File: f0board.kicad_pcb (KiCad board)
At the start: 2 copper layers, 31 x 18.3 mm, 26 parts, among them P1 CONN_12, P2 CONN_12, SW1 SW_PUSH, U1 STM32F303CCT6, U2 MCP1700, U3 MAX3051, X1 XTAL-SMD-4-PADS

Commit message: Add dimensioning.
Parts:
- moved CONN2 20.4 mm to (84.8, 87.4)
- moved U3 8.27 mm to (95.2, 82.5)
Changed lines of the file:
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@@
     (links 90)
     (no_connects 90)
-    (area 0 0 0 0)
+    (area 84.988999 57.2262 139.960595 96.841001)
     (thickness 1.6)
-    (drawings 4)
+    (drawings 6)
     (tracks 0)
     (zones 0)
@@
   )
   (module _connectors:_Molex-PicoBlade-SMD-4 (layer F.Cu)
-    (at 86.868 67.056 270)
+    (at 84.836 87.376 270)
     (fp_text reference CONN2 (at 0 -0.8 270) (layer F.SilkS)
       (effects (font (size 0.5 0.5) (thickness 0.125)))
@@
   )
   (module _std:_SOT23-8 (layer F.Cu)
-    (at 94.6785 74.295)
+    (at 95.25 82.55)
     (fp_text reference U3 (at 0.9 -1.8) (layer F.SilkS)
       (effects (font (size 0.5 0.5) (thickness 0.125)))
@@
       (net 5 "Net-(C9-Pad1)"))
   )
+  (dimension 30.988 (width 0.3) (layer Cmts.User)
+    (gr_text "30.988 mm" (at 116.84 55.038) (layer Cmts.User)
+      (effects (font (size 1.5 1.5) (thickness 0.3)))
+    )
+    (feature1 (pts (xy 132.334 59.436) (xy 132.334 53.688)))
+    (feature2 (pts (xy 101.346 59.436) (xy 101.346 53.688)))
+    (crossbar (pts (xy 101.346 56.388) (xy 132.334 56.388)))
+    (arrow1a (pts (xy 132.334 56.388) (xy 131.207496 56.974421)))
+    (arrow1b (pts (xy 132.334 56.388) (xy 131.207496 55.801579)))
+    (arrow2a (pts (xy 101.346 56.388) (xy 102.472504 56.974421)))
+    (arrow2b (pts (xy 101.346 56.388) (xy 102.472504 55.801579)))
+  )
+  (dimension 18.288 (width 0.3) (layer Cmts.User)
+    (gr_text "18.288 mm" (at 97.202 68.58 90) (layer Cmts.User)
+      (effects (font (size 1.5 1.5) (thickness 0.3)))
+    )
+    (feature1 (pts (xy 101.346 59.436) (xy 95.852 59.436)))
+    (feature2 (pts (xy 101.346 77.724) (xy 95.852 77.724)))
+    (crossbar (pts (xy 98.552 77.724) (xy 98.552 59.436)))
+    (arrow1a (pts (xy 98.552 59.436) (xy 99.138421 60.562504)))
+    (arrow1b (pts (xy 98.552 59.436) (xy 97.965579 60.562504)))
+    (arrow2a (pts (xy 98.552 77.724) (xy 99.138421 76.597496)))
+    (arrow2b (pts (xy 98.552 77.724) (xy 97.965579 76.597496)))
+  )
   (gr_line (start 101.346 77.724) (end 101.346 59.436) (angle 90) (layer Edge.Cuts) (width 0.1))

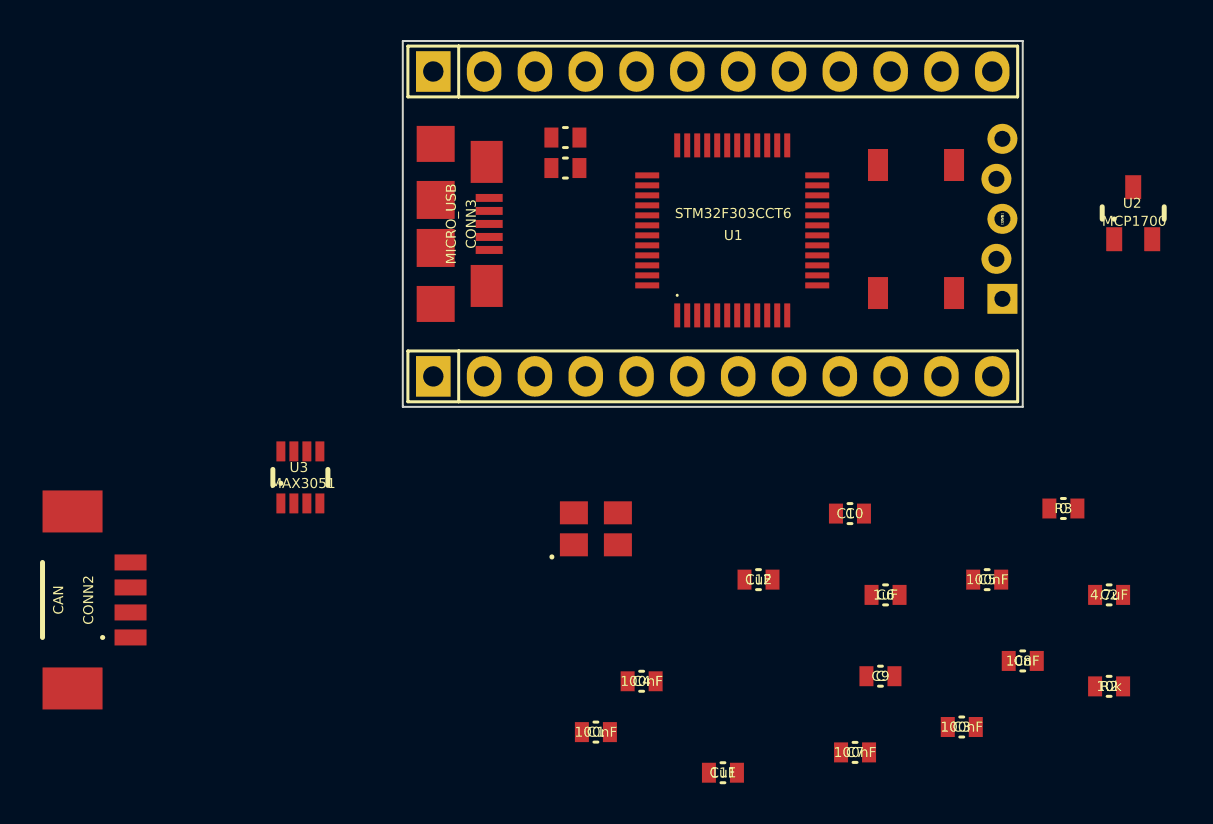
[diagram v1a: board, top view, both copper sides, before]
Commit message: placing/routing, change pinorder, add diode.
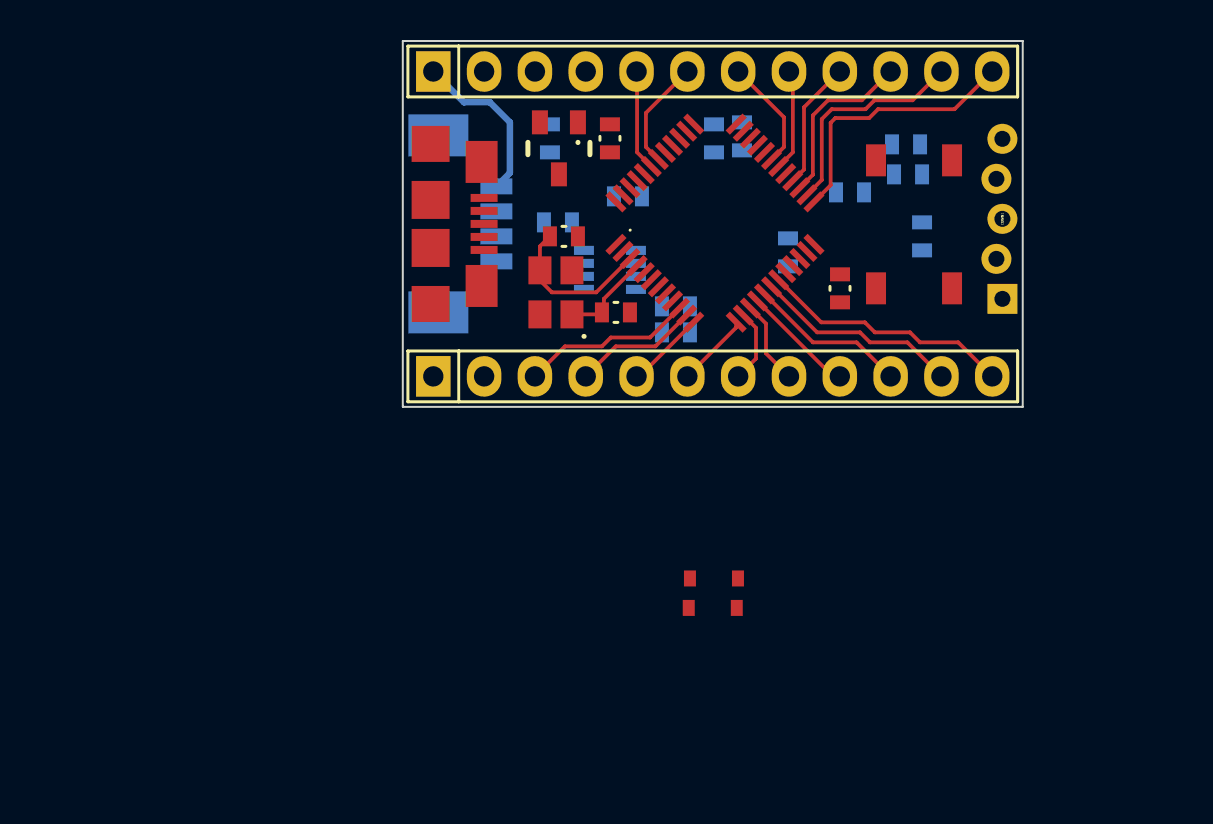
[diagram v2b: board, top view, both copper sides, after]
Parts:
- added D2: BAT60JFILM, _std:_SOD-323, F.Cu at (116.9, 86.3)
- added D3: BAT60JFILM, _std:_SOD-323, F.Cu at (116.8, 87.8)
- C1, C11, C2, C3, C4, C5, C6, C7, C8, CONN2, R1, R2, R3, U3: moved to B.Cu
- moved C1 33.2 mm to (126.5, 64.6)
- moved C11 32.9 mm to (108.7, 64.3), turned to 270 degrees
- moved C3 31.9 mm to (116.9, 64.3), turned to 270 degrees
- moved C7 30.0 mm to (112.6, 67.2)
- moved C2 29.4 mm to (118.3, 64.2), turned to 270 degrees
- moved R3 29.0 mm to (109.1, 68.5), turned to 180 degrees
- moved R2 27.5 mm to (126.6, 66.1)
- moved U2 27.4 mm to (110.1, 63.5), turned to 180 degrees
- moved C4 26.3 mm to (127.3, 69.2), turned to 270 degrees
- moved CONN2 26.2 mm to (103.1, 68.6), turned to 90 degrees
- moved C8 24.8 mm to (115.0, 72.7), turned to 180 degrees
- moved C12 23.3 mm to (111.7, 64.3), turned to 90 degrees
- moved C9 22.5 mm to (112.0, 73.0)
- moved U3 21.8 mm to (113.0, 69.9), turned to 270 degrees
- moved C10 19.9 mm to (109.4, 69.2)
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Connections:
- P1 pad 10: /PB13 -> /PB14
- P1 pad 11: /PB14 -> /PB13
- P1 pad 12: /PB15 -> /PB12
- P1 pad 5: /PA9 -> /PB7
- P1 pad 6: /PA10 -> /PB6
- P1 pad 7: /PB6 -> /PA10
- P1 pad 8: /PB7 -> /PA9
- P1 pad 9: /PB12 -> /PB15
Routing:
- net /PB12: track 0.00 -> 13.4 mm
- net /PB1: track 0.00 -> 12.7 mm
- net /PB13: track 0.00 -> 11.1 mm
- net /PB0: track 0.00 -> 10.3 mm
- net /PB14: track 0.00 -> 8.68 mm
- net /PA0: track 0.00 -> 8.65 mm
- net /5VCAN: track 0.00 -> 8.37 mm
- net /PA7: track 0.00 -> 8.01 mm
- net Net-(C10-Pad1): track 0.00 -> 7.86 mm
- net /PB15: track 0.00 -> 6.43 mm
- net /PA1: track 0.00 -> 6.31 mm
- net /PA6: track 0.00 -> 5.68 mm
- net /PA10: track 0.00 -> 5.60 mm
- net /PB6: track 0.00 -> 5.51 mm
- net /PA9: track 0.00 -> 5.13 mm
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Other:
- rule pad_to_mask_clearance: 0 -> 0.13
- rule trace_min: 0.254 -> 0.1524
- rule via_min_drill: 0.508 -> 0.3
- rule via_min_size: 0.889 -> 0.65

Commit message: Routing, change LED Pin.
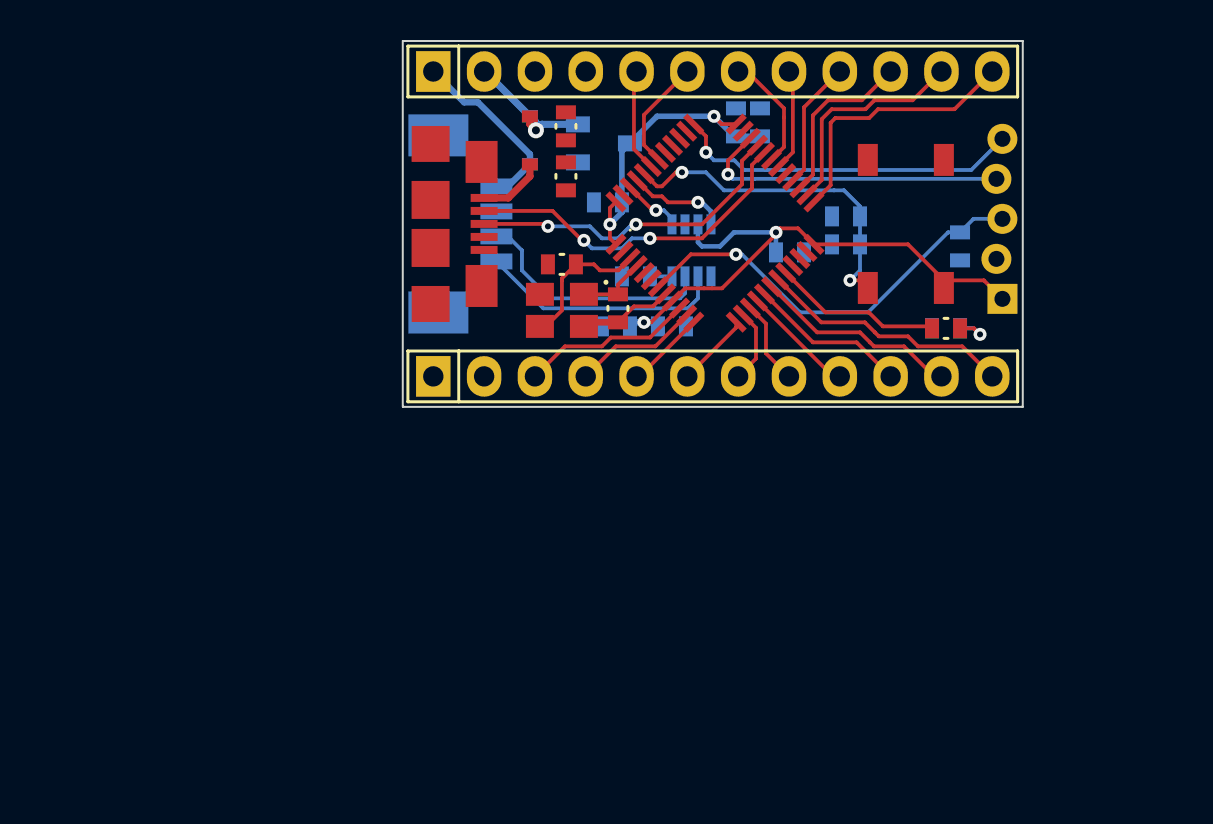
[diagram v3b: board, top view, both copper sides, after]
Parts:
- C11: moved to F.Cu
- D3, U2: moved to B.Cu
- moved D3 25.1 mm to (107.7, 64.4), turned to 90 degrees
- moved D2 23.8 mm to (107.7, 64.4), turned to 90 degrees
- moved R1 8.32 mm to (128.5, 73.8), turned to 180 degrees
- moved C1 5.83 mm to (123.5, 69.6), turned to 180 degrees
- moved D1 5.66 mm to (128.5, 73.8), turned to 0 degrees
- moved R3 4.74 mm to (113.0, 71.2)
- moved R2 3.74 mm to (123.5, 68.2), turned to 180 degrees
- moved C8 3.16 mm to (112.0, 73.7)
- moved C12 2.91 mm to (109.5, 66.2)
- moved U3 2.22 mm to (114.8, 68.6), turned to 0 degrees
- moved U2 2.00 mm to (110.1, 65.5), turned to 90 degrees
- moved C4 1.96 mm to (129.2, 69.7)
- moved C10 1.40 mm to (109.3, 70.6), turned to 180 degrees
- moved C3 1.36 mm to (118.0, 63.5), turned to 90 degrees
- moved C2 1.14 mm to (119.2, 63.5), turned to 90 degrees
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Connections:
- U1 pad 20: Net-(U1-Pad20) -> /LED
- U1 pad 40: /LED -> Net-(U1-Pad40)
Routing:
- net VCC: track 0.00 -> 45.1 mm, vias 0 -> 4
- net /RST: track 0.00 -> 21.0 mm, vias 0 -> 1
- net /SWDCLK: track 0.00 -> 17.5 mm, vias 0 -> 1
- net /USB_DM: track 0.00 -> 17.5 mm, vias 0 -> 2
- net /BOOT0: track 0.00 -> 17.4 mm, vias 0 -> 2
- net /USB_DP: track 0.00 -> 16.6 mm, vias 0 -> 2
- net /SWDIO: track 0.00 -> 15.8 mm, vias 0 -> 1
- net Net-(CONN2-Pad4): track 0.00 -> 12.4 mm
- net Net-(CONN2-Pad3): track 0.00 -> 12.2 mm
- net /LED: track 0.00 -> 8.47 mm
- net /5V: track 0.00 -> 7.09 mm, vias 0 -> 1
- net /CAN_RX: track 0.00 -> 4.97 mm, vias 0 -> 1
- net GND: track 0.00 -> 4.75 mm
- net /VUSB: track 0.00 -> 3.34 mm
- net /CAN_TX: track 0.00 -> 3.03 mm, vias 0 -> 1
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
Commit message: Big layout change, routing almost finished.
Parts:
- C1, C5, C7, R2: moved to F.Cu
- D1, SW1: moved to B.Cu
- U2: footprint _std:_SOT23-3 -> _div:_MCP1700-SOT-89; moved to F.Cu
- moved CONN1 28.7 mm to (102.6, 68.6)
- moved CONN2 27.2 mm to (130.3, 68.6), turned to 270 degrees
- moved CONN3 22.9 mm to (128.3, 68.6), turned to 90 degrees
- moved D2 19.4 mm to (125.9, 71.2), turned to 270 degrees
- moved SW1 19.0 mm to (107.5, 68.6)
- moved C4 16.0 mm to (113.3, 71.2), turned to 180 degrees
- moved D3 14.6 mm to (121.0, 70.4), turned to 180 degrees
- moved C1 13.1 mm to (111.4, 64.5)
- moved R2 13.1 mm to (111.4, 63.2)
- moved R3 12.3 mm to (124.3, 66.4)
- moved R1 9.90 mm to (118.6, 73.9)
- moved U3 8.68 mm to (122.7, 65.0), turned to 90 degrees
- moved D1 7.50 mm to (121.0, 73.9), turned to 180 degrees
- moved U2 4.72 mm to (105.7, 67.2), turned to 0 degrees
- moved C11 4.62 mm to (104.9, 63.3), turned to 180 degrees
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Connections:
- CONN2 pad MECH: GND -> (no net)
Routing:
- net GND: track 4.75 -> 63.2 mm, vias 0 -> 7
- net /5V: track 7.09 -> 37.4 mm, vias 1 -> 2
- net VCC: track 45.1 -> 72.2 mm, vias 4 -> 3
- net /5VCAN: track 9.18 -> 36.0 mm, vias 0 -> 2
- net /BOOT0: track 17.4 -> 7.27 mm, vias 2 -> 1
- net /CAN_TX: track 3.03 -> 11.4 mm
- net Net-(CONN2-Pad4): track 12.4 -> 4.40 mm
- net /CAN_RX: track 4.97 -> 12.6 mm
- net Net-(CONN2-Pad3): track 12.2 -> 5.40 mm
- net /USB_DM: track 17.5 -> 11.9 mm, vias 2 -> 0
- net /RST: track 21.0 -> 15.8 mm
- net /SWDIO: track 15.8 -> 20.2 mm
- net /LED: track 8.47 -> 4.47 mm, vias 0 -> 1
- net /USB_DP: track 16.6 -> 12.9 mm
- net /SWDCLK: track 17.5 -> 20.4 mm
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- added copper zone on B.Cu, net GND
- added copper zone on F.Cu, net GND

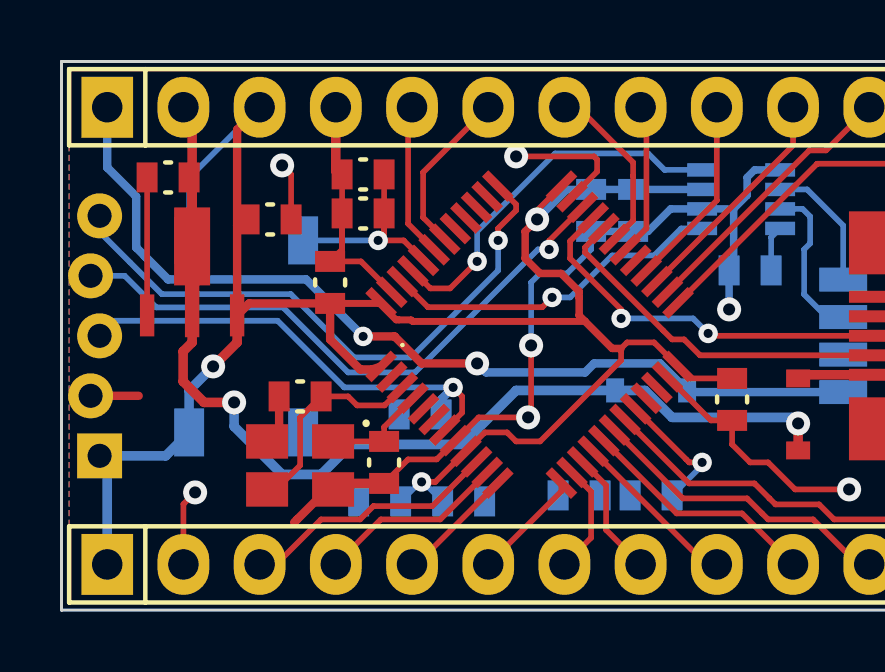
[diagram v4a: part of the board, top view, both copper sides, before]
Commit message: Add missing connection to LED, improved GND and VCC routing.
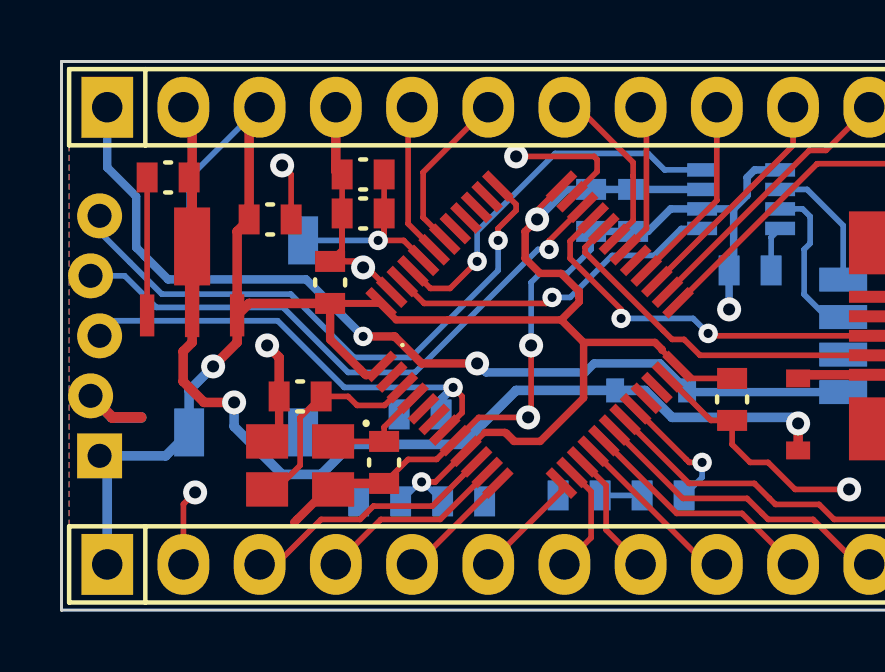
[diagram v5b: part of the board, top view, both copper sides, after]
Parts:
- moved D1 0.40 mm to (121.4, 73.9)
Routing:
- net GND: track 63.2 -> 68.7 mm, vias 7 -> 9
- net VCC: track 72.2 -> 75.1 mm
- net Net-(D1-Pad2): track 0.00 -> 1.40 mm

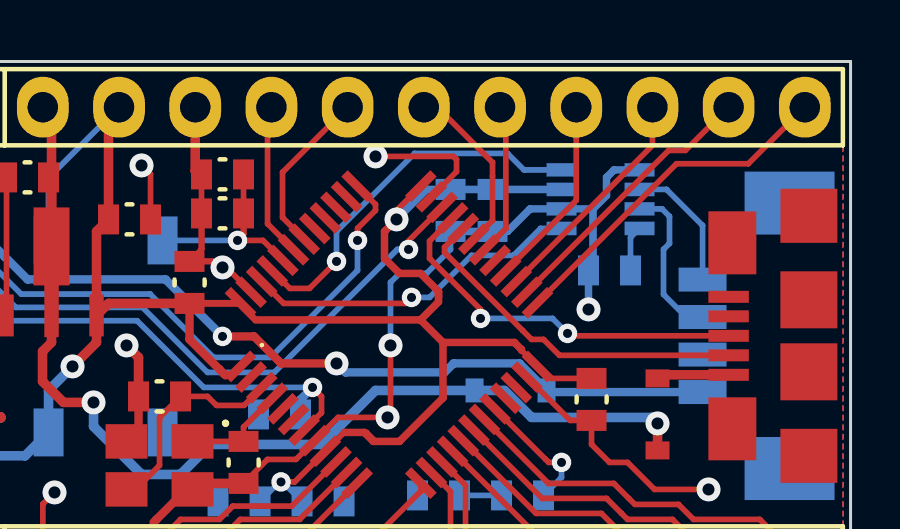
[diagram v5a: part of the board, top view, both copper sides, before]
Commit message: Improve GND connection.
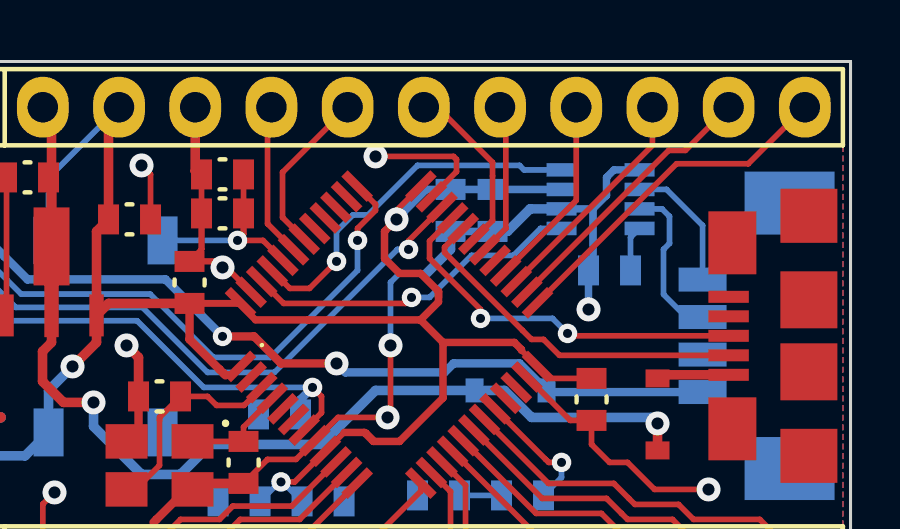
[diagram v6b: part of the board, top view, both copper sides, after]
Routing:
- net GND: track 68.7 -> 71.3 mm
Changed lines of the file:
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@@
   (general
     (links 93)
-    (no_connects 2)
+    (no_connects 1)
     (area 90.552001 53.538 132.593643 77.799001)
     (thickness 1.6)
     (drawings 6)
-    (tracks 365)
+    (tracks 370)
     (zones 0)
     (modules 28)
@@
   )
   (setup
-    (last_trace_width 0.254)
+    (last_trace_width 0.19)
     (user_trace_width 0.17)
     (user_trace_width 0.19)
@@
   (gr_line (start 132.334 59.436) (end 132.334 77.724) (angle 90) (layer Edge.Cuts) (width 0.1))
   (gr_line (start 101.346 59.436) (end 132.334 59.436) (angle 90) (layer Edge.Cuts) (width 0.1))
+  (segment (start 119 65.1) (end 119 65.7) (width 0.32) (layer B.Cu) (net 1))
+  (segment (start 119 65.7) (end 118.2 66.5) (width 0.32) (layer B.Cu) (net 1))
+  (segment (start 122.7 64.35) (end 121.65 64.35) (width 0.32) (layer B.Cu) (net 1))
+  (segment (start 121.65 64.35) (end 120.9 65.1) (width 0.32) (layer B.Cu) (net 1))
+  (segment (start 120.9 65.1) (end 120.4 65.1) (width 0.32) (layer B.Cu) (net 1))
   (segment (start 123.6 67.7) (end 123.6 66.4) (width 0.25) (layer B.Cu) (net 1))
   (via (at 123.6 67.7) (size 0.8) (drill 0.4) (layers F.Cu B.Cu) (net 1))
@@
   (segment (start 117 66.8) (end 117 68.9) (width 0.19) (layer B.Cu) (net 1))
   (via (at 117 68.9) (size 0.8) (drill 0.4) (layers F.Cu B.Cu) (net 1))
-  (segment (start 119 65.7) (end 119 65.1) (width 0.19) (layer B.Cu) (net 1))
   (segment (start 117 71.2) (end 116.9 71.3) (width 0.19) (layer F.Cu) (net 1))
   (via (at 116.5 62.6) (size 0.8) (drill 0.4) (layers F.Cu B.Cu) (net 1))
@@
   (segment (start 110.49 63.09) (end 110.7 63.3) (width 0.32) (layer F.Cu) (net 1))
   (segment (start 110.2 73.7) (end 109.1 74.8) (width 0.19) (layer F.Cu) (net 1))
-  (segment (start 122.7 64.35) (end 121.65 64.35) (width 0.25) (layer B.Cu) (net 1))
   (segment (start 121.65 64.35) (end 120.9 65.1) (width 0.25) (layer B.Cu) (net 1))
   (segment (start 120.9 65.1) (end 119 65.1) (width 0.25) (layer B.Cu) (net 1))
@@
   (segment (start 125.3 65) (end 125 65.3) (width 0.19) (layer B.Cu) (net 38))
   (segment (start 125 65.3) (end 125 66.4) (width 0.19) (layer B.Cu) (net 38))
+  (segment (start 122.7 63.05) (end 121.45 63.05) (width 0.19) (layer B.Cu) (net 48))
+  (segment (start 121.45 63.05) (end 121.3 62.9) (width 0.19) (layer B.Cu) (net 48))
+  (segment (start 116.25 64.55) (end 115.75 64.55) (width 0.19) (layer B.Cu) (net 48))
+  (segment (start 117.9 62.9) (end 116.25 64.55) (width 0.19) (layer B.Cu) (net 48))
+  (segment (start 121.3 62.9) (end 117.9 62.9) (width 0.19) (layer B.Cu) (net 48))
   (segment (start 113.06066 66.418019) (end 113.642641 67) (width 0.19) (layer F.Cu) (net 48))
-  (segment (start 117.8 62.5) (end 120.9 62.5) (width 0.19) (layer B.Cu) (net 48))
-  (segment (start 115.2 65.1) (end 117.8 62.5) (width 0.19) (layer B.Cu) (net 48))
+  (segment (start 115.2 65.1) (end 115.75 64.55) (width 0.19) (layer B.Cu) (net 48))
   (segment (start 115.2 66.1) (end 115.2 65.1) (width 0.19) (layer B.Cu) (net 48))
   (via (at 115.2 66.1) (size 0.65) (drill 0.3) (layers F.Cu B.Cu) (net 48))
   (segment (start 114.3 67) (end 115.2 66.1) (width 0.19) (layer F.Cu) (net 48))
   (segment (start 113.642641 67) (end 114.3 67) (width 0.19) (layer F.Cu) (net 48))
-  (segment (start 122.7 63.05) (end 121.45 63.05) (width 0.19) (layer B.Cu) (net 48))
-  (segment (start 121.45 63.05) (end 120.9 62.5) (width 0.19) (layer B.Cu) (net 48))
   (segment (start 118.3 67.3) (end 119.7 65.9) (width 0.19) (layer B.Cu) (net 49))
   (segment (start 117.7 67.3) (end 118.3 67.3) (width 0.19) (layer B.Cu) (net 49))
